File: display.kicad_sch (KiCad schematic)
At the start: 11 parts, among them U4 SSD1306

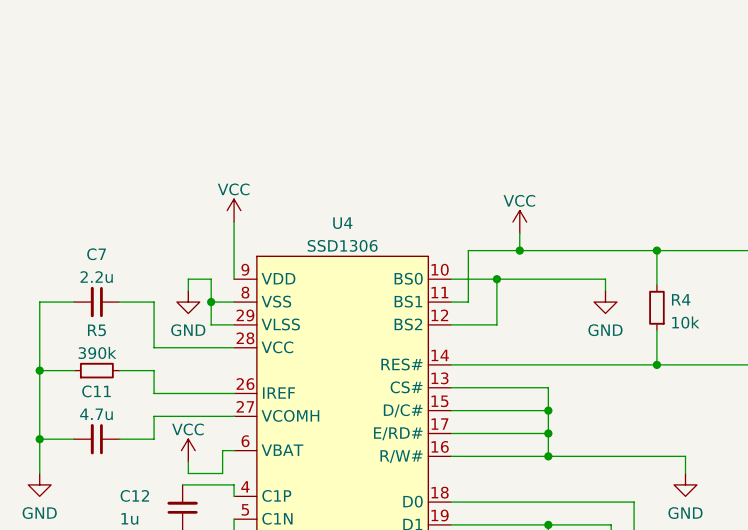
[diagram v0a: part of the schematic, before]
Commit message: Add board REV-D
Revision D changes the mounting holes so that we can fit screws to
assemble the two case pieces.

Also add required compliance logos on the back.
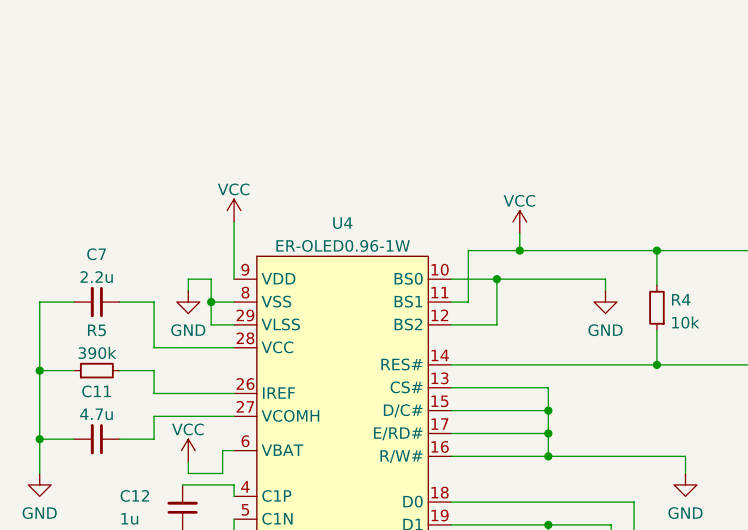
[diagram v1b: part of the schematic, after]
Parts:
- U4: value SSD1306 -> ER-OLED0.96-1W
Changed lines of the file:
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@@
       (effects (font (size 1.27 1.27)))
     )
-    (property "Value" "SSD1306" (at 145.415 70.0079 0)
+    (property "Value" "ER-OLED0.96-1W" (at 145.415 70.0079 0)
       (effects (font (size 1.27 1.27)))
     )
